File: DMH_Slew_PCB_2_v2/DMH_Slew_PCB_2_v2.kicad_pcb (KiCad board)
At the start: 2 copper layers, 48 x 175 mm, 0 parts

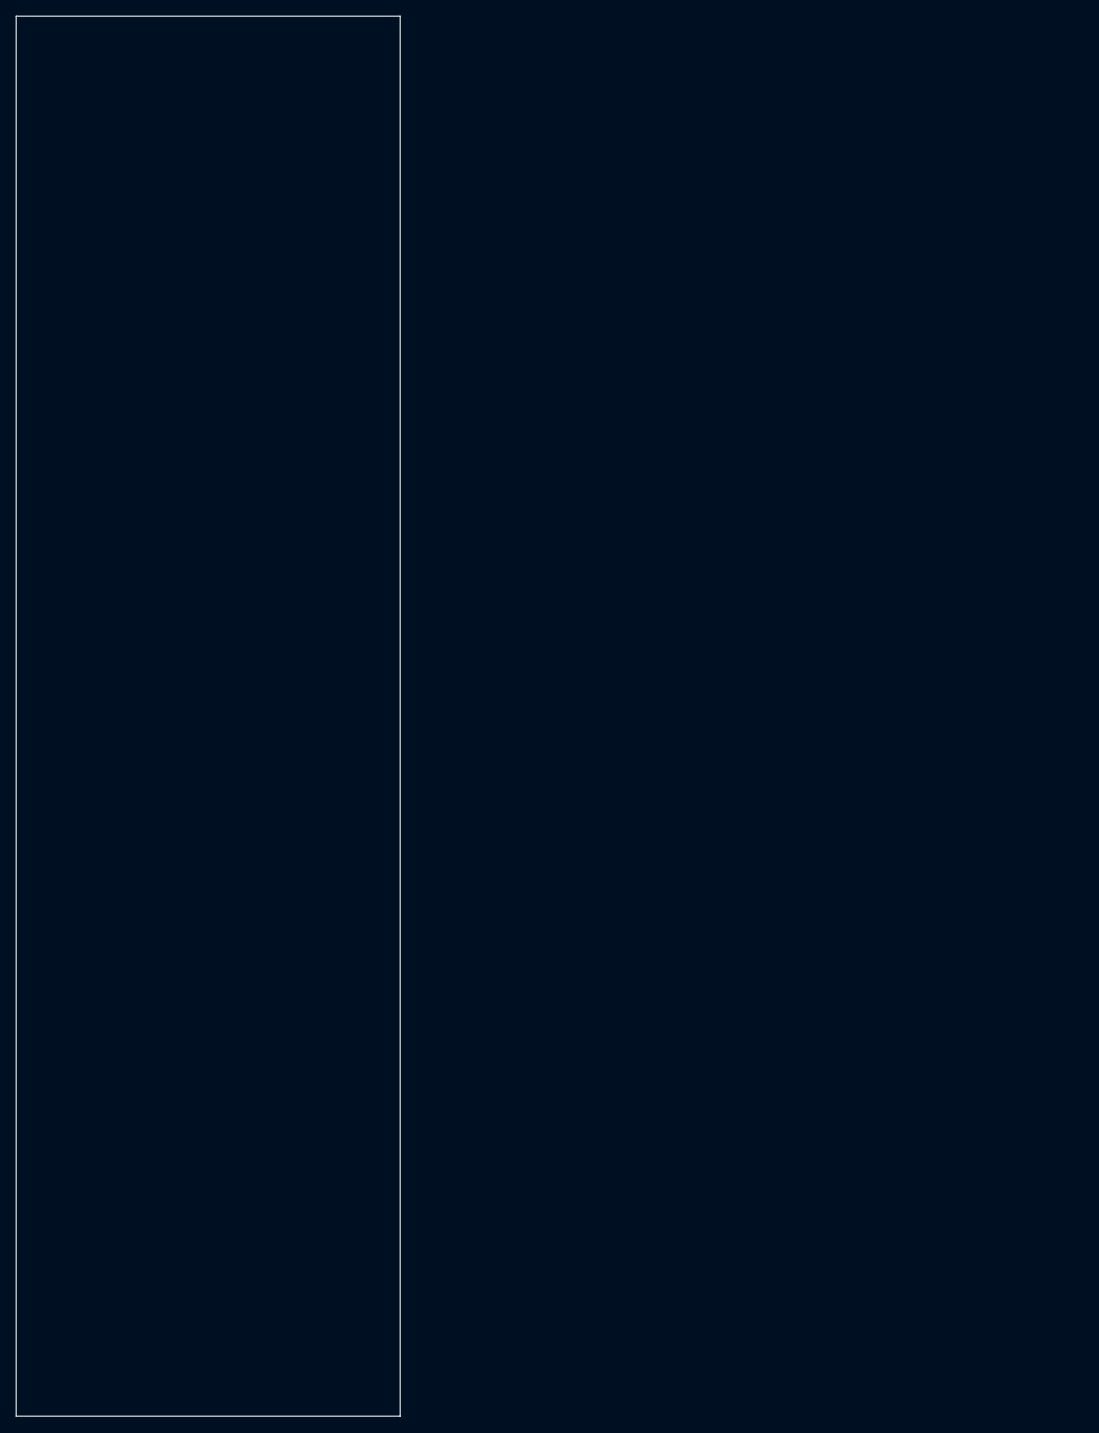
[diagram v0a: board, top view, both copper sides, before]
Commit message: Started PCB 2 component placement
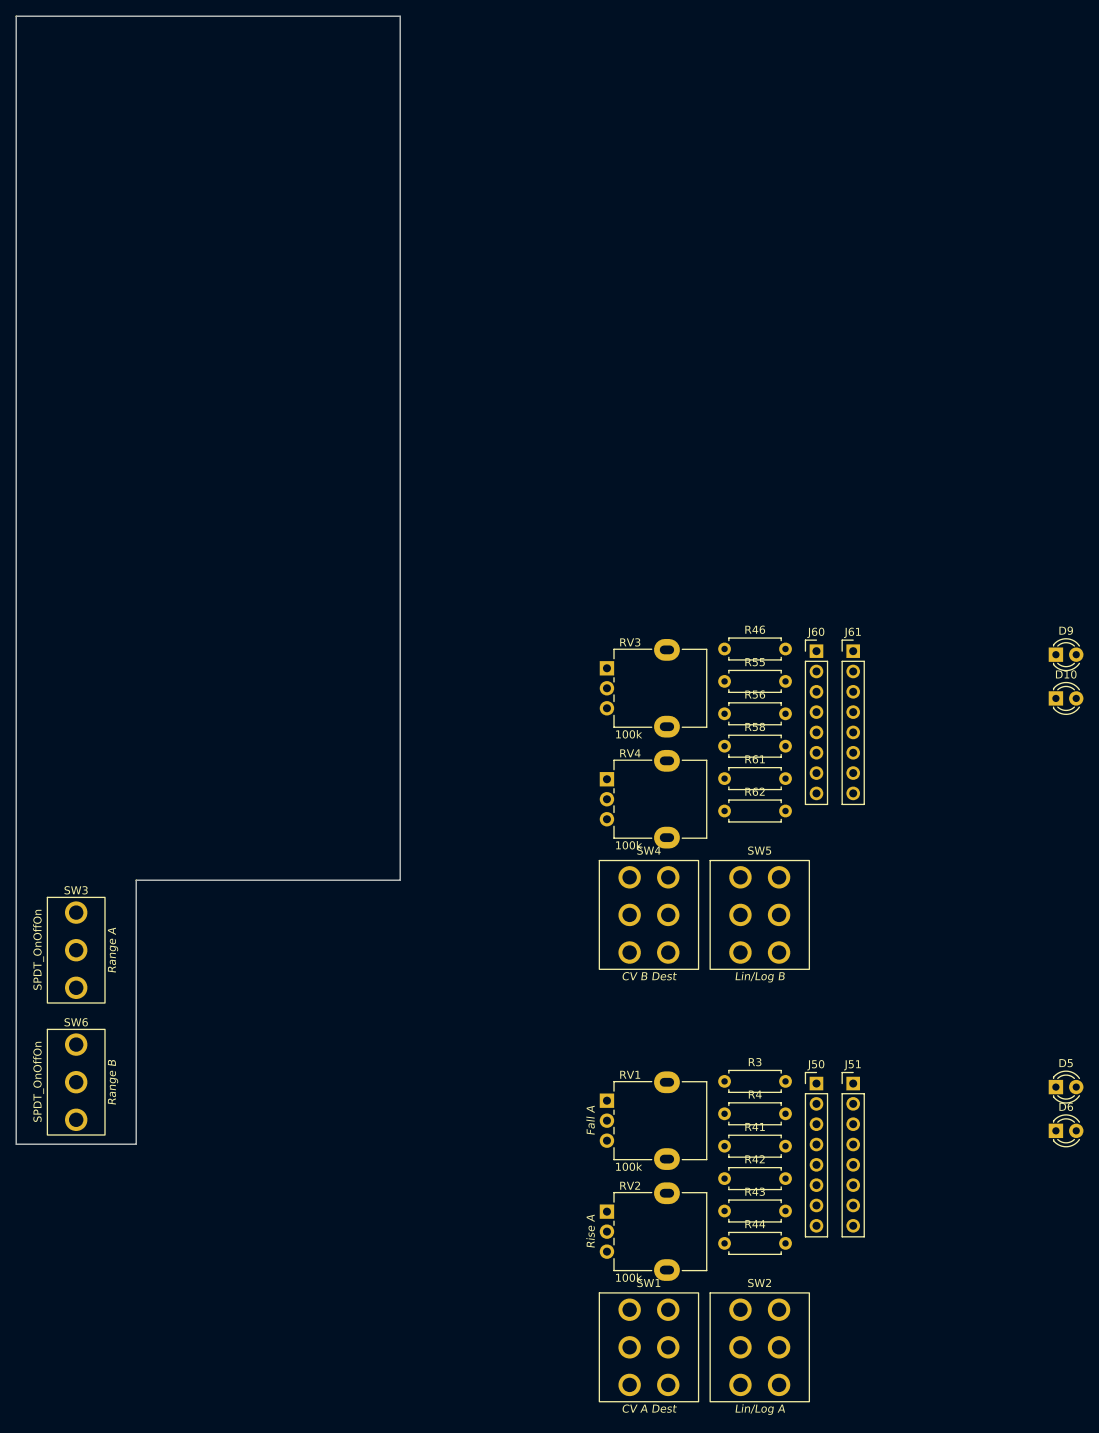
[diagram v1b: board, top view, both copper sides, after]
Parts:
- added D10: LED_B_R, LED_THT:LED_D3.0mm, F.Cu at (181.0, 127.8)
- added D5: LED_A_Y, LED_THT:LED_D3.0mm, F.Cu at (181.0, 176.4)
- added D6: LED_A_R, LED_THT:LED_D3.0mm, F.Cu at (181.0, 181.8)
- added D9: LED_B_Y, LED_THT:LED_D3.0mm, F.Cu at (181.0, 122.3)
- added J50: Conn_01x08_PinHeader, Connector_PinHeader_2.54mm:PinHeader_1x08_P2.54mm_Vertical, F.Cu at (151.0, 175.9)
- added J51: Conn_01x08_PinHeader, Connector_PinHeader_2.54mm:PinHeader_1x08_P2.54mm_Vertical, F.Cu at (155.6, 175.9)
- added J60: Conn_01x08_PinHeader, Connector_PinHeader_2.54mm:PinHeader_1x08_P2.54mm_Vertical, F.Cu at (151.0, 121.9)
- added J61: Conn_01x08_PinHeader, Connector_PinHeader_2.54mm:PinHeader_1x08_P2.54mm_Vertical, F.Cu at (155.6, 121.9)
- added R3: 56k, Resistor_THT:R_Axial_DIN0207_L6.3mm_D2.5mm_P7.62mm_Horizontal, F.Cu at (139.5, 175.7)
- added R4: 56k, Resistor_THT:R_Axial_DIN0207_L6.3mm_D2.5mm_P7.62mm_Horizontal, F.Cu at (139.5, 179.7)
- added R41: 5k1, Resistor_THT:R_Axial_DIN0207_L6.3mm_D2.5mm_P7.62mm_Horizontal, F.Cu at (139.5, 183.8)
- added R42: 5k1, Resistor_THT:R_Axial_DIN0207_L6.3mm_D2.5mm_P7.62mm_Horizontal, F.Cu at (139.5, 187.8)
- added R43: 5k1, Resistor_THT:R_Axial_DIN0207_L6.3mm_D2.5mm_P7.62mm_Horizontal, F.Cu at (139.5, 191.8)
- added R44: 5k1, Resistor_THT:R_Axial_DIN0207_L6.3mm_D2.5mm_P7.62mm_Horizontal, F.Cu at (139.5, 195.9)
- added R46: 56k, Resistor_THT:R_Axial_DIN0207_L6.3mm_D2.5mm_P7.62mm_Horizontal, F.Cu at (139.5, 121.6)
- added R55: 5k1, Resistor_THT:R_Axial_DIN0207_L6.3mm_D2.5mm_P7.62mm_Horizontal, F.Cu at (139.5, 125.7)
- added R56: 5k1, Resistor_THT:R_Axial_DIN0207_L6.3mm_D2.5mm_P7.62mm_Horizontal, F.Cu at (139.5, 129.7)
- added R58: 56k, Resistor_THT:R_Axial_DIN0207_L6.3mm_D2.5mm_P7.62mm_Horizontal, F.Cu at (139.5, 133.8)
- added R61: 5k1, Resistor_THT:R_Axial_DIN0207_L6.3mm_D2.5mm_P7.62mm_Horizontal, F.Cu at (139.5, 137.8)
- added R62: 5k1, Resistor_THT:R_Axial_DIN0207_L6.3mm_D2.5mm_P7.62mm_Horizontal, F.Cu at (139.5, 141.8)
- added RV1: 100k, SynthStuff:Potentiometer_Alpha_RD901F-40-00D_Single_Vertical, F.Cu at (124.8, 178.1)
- added RV2: 100k, SynthStuff:Potentiometer_Alpha_RD901F-40-00D_Single_Vertical, F.Cu at (124.8, 191.9)
- added RV3: 100k, SynthStuff:Potentiometer_Alpha_RD901F-40-00D_Single_Vertical, F.Cu at (124.8, 124.0)
- added RV4: 100k, SynthStuff:Potentiometer_Alpha_RD901F-40-00D_Single_Vertical, F.Cu at (124.8, 137.9)
- added SW1: SW_DPDT_3way, SynthStuff:Toggle_Switch_2_Poles_TE, F.Cu at (130.1, 208.9)
- added SW2: SW_DPDT, SynthStuff:Toggle_Switch_2_Poles_TE, F.Cu at (143.9, 208.9)
- added SW3: SPDT_OnOffOn, SynthStuff:Toggle_Switch_TE, F.Cu at (58.5, 159.2)
- added SW4: SW_DPDT_3way, SynthStuff:Toggle_Switch_2_Poles_TE, F.Cu at (130.1, 154.8)
- added SW5: SW_DPDT, SynthStuff:Toggle_Switch_2_Poles_TE, F.Cu at (143.9, 154.8)
- added SW6: SPDT_OnOffOn, SynthStuff:Toggle_Switch_TE, F.Cu at (58.5, 175.8)
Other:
- board size 48 x 175 mm -> 48 x 141 mm

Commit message: PCB 2 component placement done
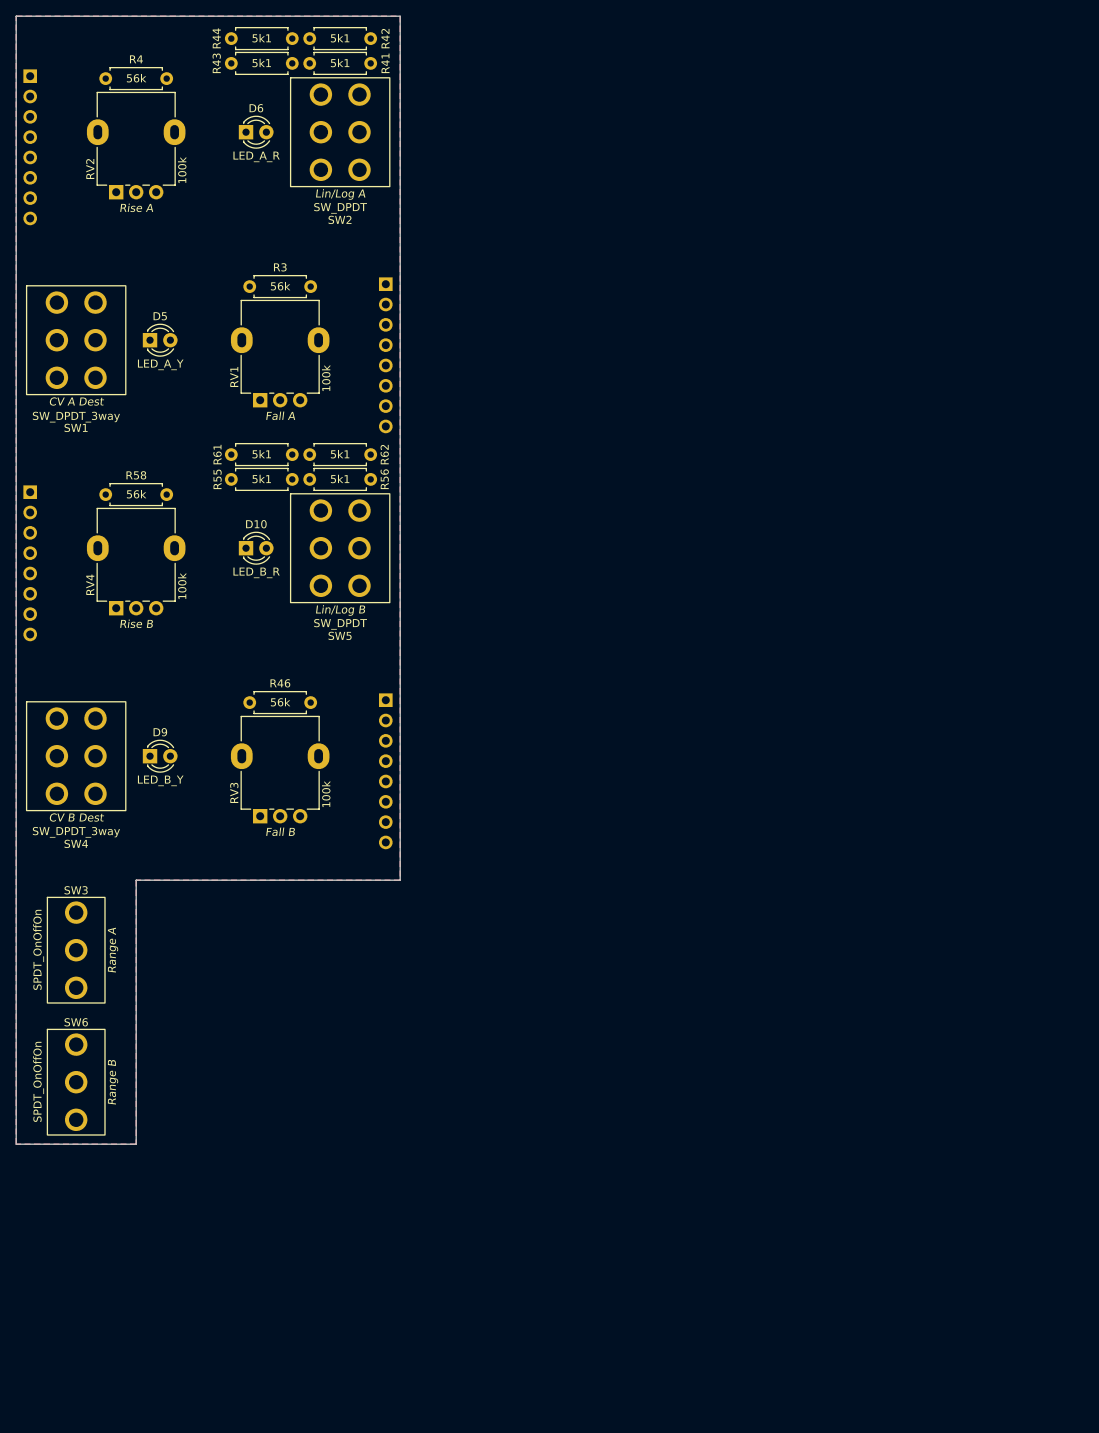
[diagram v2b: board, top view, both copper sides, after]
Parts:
- J50, J51, J60, J61: footprint Connector_PinHeader_2.54mm:PinHeader_1x08_P2.54mm_Vertical -> Connector_PinSocket_2.54mm:PinSocket_1x08_P2.54mm_Vertical; moved to B.Cu
- moved D6 160.7 mm to (79.7, 57.0)
- moved SW2 160.7 mm to (91.5, 57.0)
- moved R44 160.0 mm to (85.5, 45.3), turned to 180 degrees
- moved J50 159.7 mm to (52.8, 50.0), turned to 180 degrees
- moved R43 156.1 mm to (77.9, 48.4)
- moved R4 150.8 mm to (62.2, 50.3)
- moved R42 149.2 mm to (95.3, 45.3), turned to 180 degrees
- moved D5 146.8 mm to (67.7, 83.0)
- moved R41 144.9 mm to (87.7, 48.4)
- moved SW1 144.8 mm to (58.5, 83.0)
- moved RV2 141.4 mm to (63.5, 64.5), turned to 90 degrees
- moved J51 115.7 mm to (97.2, 76.0), turned to 180 degrees
- moved R3 115.7 mm to (80.2, 76.3)
- moved D9 113.9 mm to (67.7, 135.0)
- moved D10 103.0 mm to (79.7, 109.0)
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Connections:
- J50 pad 2: +10V_A -> Net-(J50B-Pin_2)
- J50 pad 3: Net-(J50C-Pin_3) -> /Core Circuit A/Rise_CV
- J50 pad 5: /Core Circuit A/Rise_CV -> +10V_A
- J51 pad 3: /Core Circuit A/Output -> Net-(D6-A)
- J51 pad 4: Net-(J51D-Pin_4) -> Net-(D5-A)
- J51 pad 6: Net-(D5-A) -> /Core Circuit A/Output
- J51 pad 7: Net-(D6-A) -> Net-(J51G-Pin_7)
- J60 pad 2: +10V_B -> Net-(J60B-Pin_2)
- J60 pad 3: Net-(J60C-Pin_3) -> /Core Circuit B/Rise_CV
- J60 pad 5: /Core Circuit B/Rise_CV -> +10V_B
- J61 pad 3: /Core Circuit B/Output -> Net-(D10-A)
- J61 pad 4: Net-(J61D-Pin_4) -> Net-(D9-A)
- J61 pad 6: Net-(D9-A) -> /Core Circuit B/Output
- J61 pad 7: Net-(D10-A) -> Net-(J61G-Pin_7)
- R43 pad 1: Net-(J50F-Pin_6) -> Net-(J50B-Pin_2)
- R55 pad 1: Net-(J60F-Pin_6) -> Net-(J60B-Pin_2)
- SW1 pad 3: Net-(J50C-Pin_3) -> Net-(J50F-Pin_6)
- SW1 pad 4: Net-(J50C-Pin_3) -> Net-(J50F-Pin_6)
- SW2 pad 1: Net-(J50F-Pin_6) -> Net-(J50B-Pin_2)
- SW2 pad 2: Net-(J51A-Pin_1) -> Net-(J51B-Pin_2)
- SW2 pad 5: Net-(J51B-Pin_2) -> Net-(J51A-Pin_1)
- SW3 pad 1: Net-(J51E-Pin_5) -> Net-(J51G-Pin_7)
- SW3 pad 3: Net-(J51D-Pin_4) -> Net-(J51E-Pin_5)
- SW4 pad 3: Net-(J60C-Pin_3) -> Net-(J60F-Pin_6)
- SW4 pad 4: Net-(J60C-Pin_3) -> Net-(J60F-Pin_6)
- SW5 pad 1: Net-(J60F-Pin_6) -> Net-(J60B-Pin_2)
- SW5 pad 2: Net-(J61A-Pin_1) -> Net-(J61B-Pin_2)
- SW5 pad 5: Net-(J61B-Pin_2) -> Net-(J61A-Pin_1)
- SW6 pad 1: Net-(J61E-Pin_5) -> Net-(J61G-Pin_7)
- SW6 pad 3: Net-(J61D-Pin_4) -> Net-(J61E-Pin_5)
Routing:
- added copper zone on B.Cu, net GND
- added copper zone on F.Cu, net GND

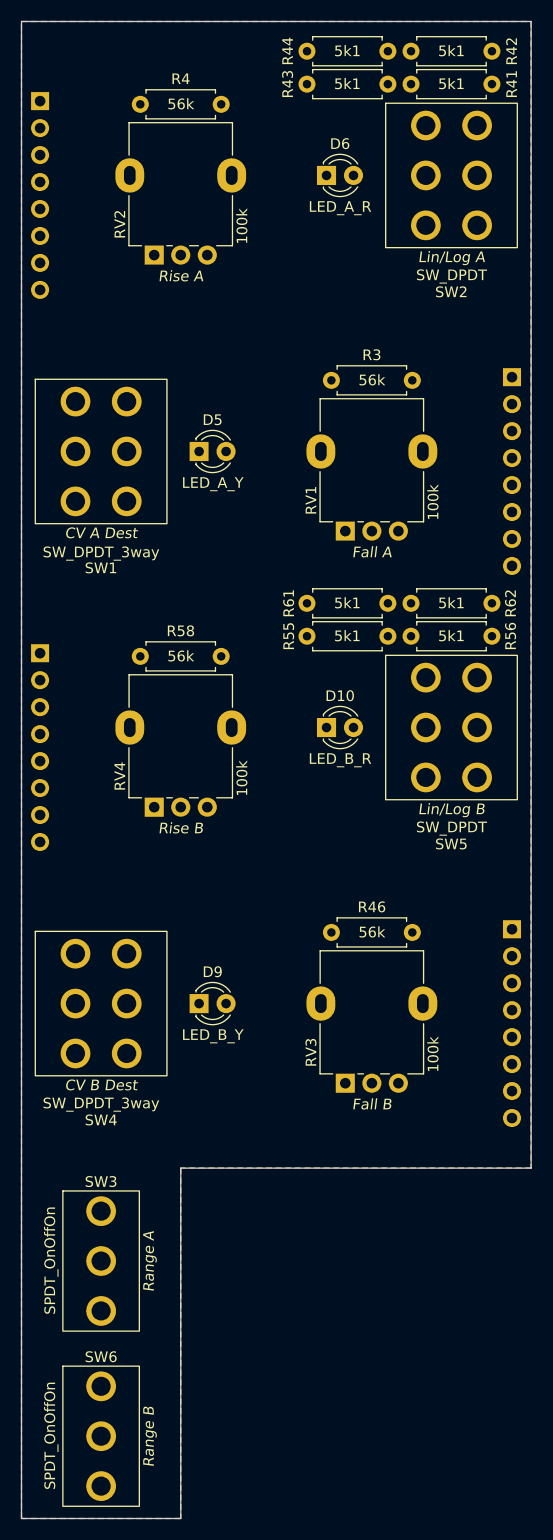
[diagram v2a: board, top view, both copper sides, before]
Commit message: PCB 2 first routing done
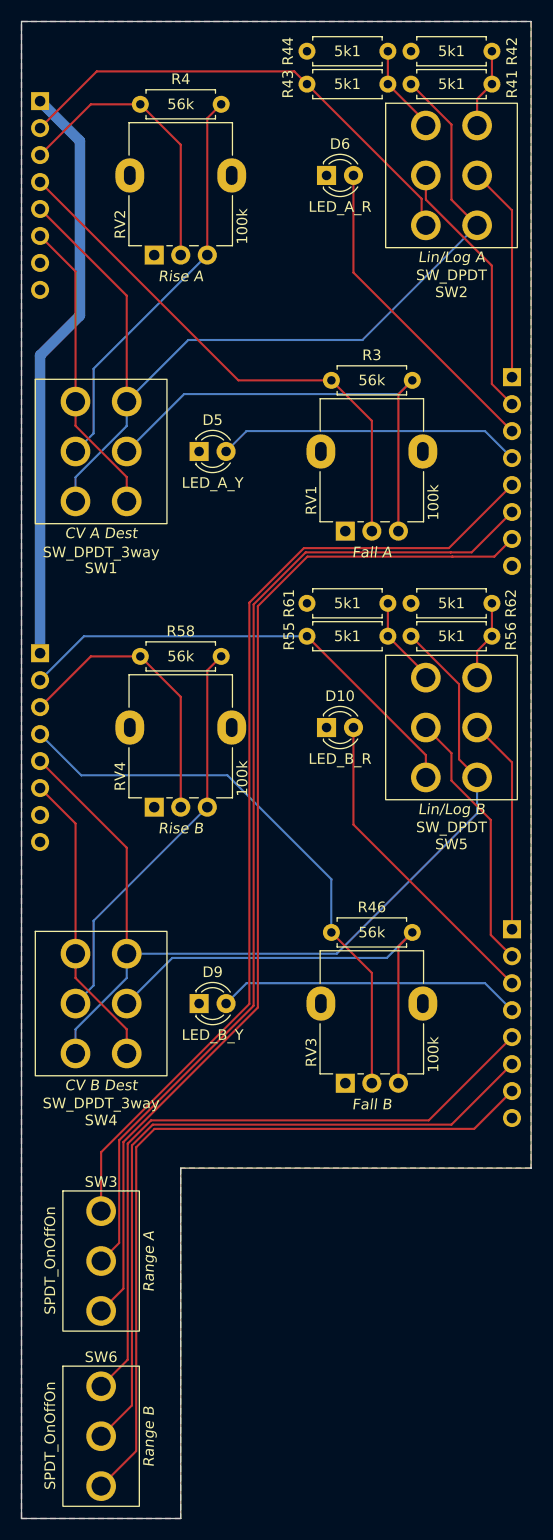
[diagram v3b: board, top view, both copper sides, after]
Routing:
- net Net-(J51G-Pin_7): track 0.00 -> 99.1 mm
- net /Core Circuit A/Output: track 0.00 -> 95.7 mm
- net Net-(J51E-Pin_5): track 0.00 -> 92.4 mm
- net +10V_B: track 0.00 -> 90.7 mm
- net +10V_A: track 0.00 -> 88.7 mm
- net Net-(J61G-Pin_7): track 0.00 -> 70.9 mm
- net /Core Circuit B/Output: track 0.00 -> 67.6 mm
- net Net-(J61E-Pin_5): track 0.00 -> 64.2 mm
- net +12V: track 0.00 -> 55.1 mm
- net /Core Circuit B/Fall_CV: track 0.00 -> 53.9 mm
- net /Core Circuit A/Fall_CV: track 0.00 -> 51.0 mm
- net Net-(J50B-Pin_2): track 0.00 -> 45.8 mm
- net Net-(J60B-Pin_2): track 0.00 -> 44.8 mm
- net Net-(R3-Pad2): track 0.00 -> 44.4 mm
- net Net-(R46-Pad2): track 0.00 -> 44.4 mm
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
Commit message: Updated Log circuit
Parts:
- removed R41, R42, R43, R44, R55, R56, R61, R62: 5k1, Resistor_THT:R_Axial_DIN0207_L6.3mm_D2.5mm_P7.62mm_Horizontal
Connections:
- J50 pad 1: +12V -> GND
- J60 pad 1: +12V -> GND
- SW2 pad 3: Net-(R43-Pad2) -> GND
- SW2 pad 6: Net-(R41-Pad2) -> GND
- SW5 pad 3: Net-(R55-Pad2) -> GND
- SW5 pad 6: Net-(R56-Pad2) -> GND
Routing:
- net +12V: track 55.1 -> 0.00 mm
- net +10V_A: track 88.7 -> 72.8 mm
- net +10V_B: track 90.7 -> 77.3 mm
- net Net-(R55-Pad2): track 8.48 -> 0.00 mm
- net Net-(R43-Pad2): track 8.48 -> 0.00 mm
- net Net-(R56-Pad2): track 7.58 -> 0.00 mm
- net Net-(R41-Pad2): track 7.58 -> 0.00 mm
- net Net-(J51G-Pin_7): track 99.1 -> 97.0 mm
- net /Core Circuit A/Output: track 95.7 -> 93.7 mm
- net Net-(J51E-Pin_5): track 92.4 -> 90.4 mm
- net Net-(D5-A): track 28.8 -> 29.8 mm
- net Net-(D9-A): track 28.8 -> 29.7 mm
